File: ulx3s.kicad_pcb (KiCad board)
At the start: 4 copper layers, 94 x 50.8 mm, 119 parts, among them J1 CONN_02X20, J2 CONN_02X20, J3 WIFI_OFF, J4 CONN_02X03, Q1 BC857, Q2 2N7002, U10 S25FL164K0XMFI011, U11 PCA9306DCTR, U2 ESP-32S, U3 AP3429A, U4 AP3429A, U5 AP3429A, U6 FT231XS, U7 PCF8523, U8 MAX11123, U9 MT48LC4M16A2TG, Y1 FNETHE025

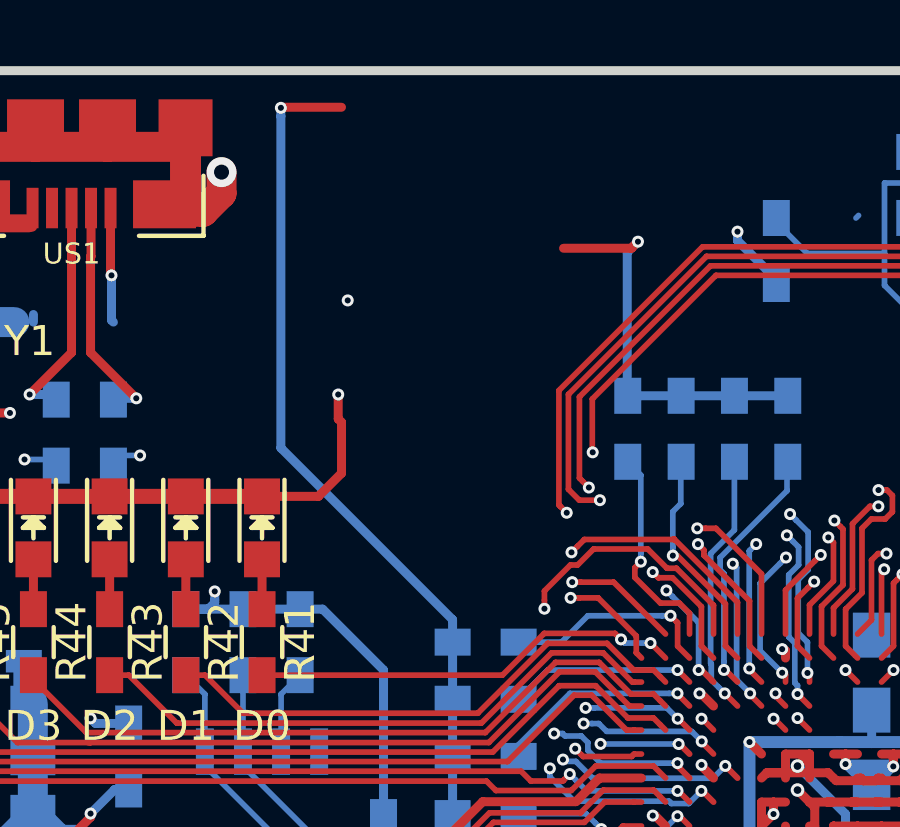
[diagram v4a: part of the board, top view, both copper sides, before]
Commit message: PCB v1.7 fix wrong audio jack connection
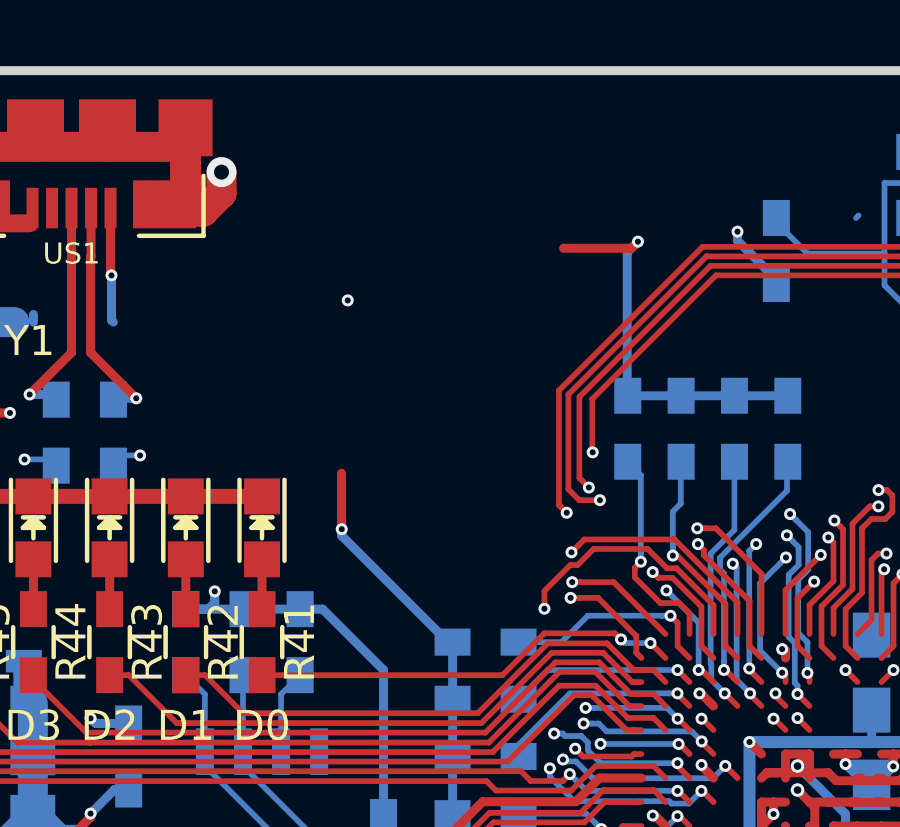
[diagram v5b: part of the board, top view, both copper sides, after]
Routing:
- net /analog/AUDIO_L: track 27.9 -> 13.0 mm
- net GND: track 360.3 -> 354.6 mm, vias 52 -> 51
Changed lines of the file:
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@@
     (links 708)
     (no_connects 0)
-    (area 71.010001 43.48 197.572001 118.732339)
+    (area 93.949999 61.269999 188.230001 112.370001)
     (thickness 1.6)
     (drawings 28)
-    (tracks 4123)
+    (tracks 4115)
     (zones 0)
     (modules 160)
@@
     (fp_line (start -7 -3) (end -5.6 -3) (layer F.SilkS) (width 0.15))
     (pad 1 smd rect (at -6.4 3.7 270) (size 2.2 2.8) (layers F.Cu F.Paste F.Mask)
-      (net 34 /analog/AUDIO_L))
+      (net 1 GND))
     (pad 4 smd rect (at -3.6 3.7 270) (size 2.2 2.8) (layers F.Cu F.Paste F.Mask))
     (pad 2 smd rect (at 5.8 3.7 270) (size 2.8 2.8) (layers F.Cu F.Paste F.Mask)
-      (net 1 GND))
+      (net 34 /analog/AUDIO_L))
     (pad 5 smd rect (at 9.9 -0.75 270) (size 2.8 2.8) (layers F.Cu F.Paste F.Mask))
     (pad 3 smd rect (at -1.7 -3.7 270) (size 2 2.8) (layers F.Cu F.Paste F.Mask)
@@
     (effects (font (size 1.5 1.5) (thickness 0.3)) (justify mirror))
   )
-  (gr_text "ULX3S v1.6" (at 138.55 75.898) (layer F.SilkS)
+  (gr_text "ULX3S v1.7" (at 138.55 75.898) (layer F.SilkS)
     (effects (font (size 1.5 1.5) (thickness 0.3)))
   )
@@
   (segment (start 131.68 89) (end 131.28 89.4) (width 0.3) (layer F.Cu) (net 1))
   (via (at 131.28 89.450837) (size 0.4) (drill 0.2) (layers F.Cu B.Cu) (net 1))
-  (via (at 120.77 72.215) (size 0.4) (drill 0.2) (layers F.Cu B.Cu) (net 1))
-  (segment (start 120.88 74.84) (end 120.88 73.14) (width 0.3) (layer F.Cu) (net 1))
-  (segment (start 120.88 73.14) (end 120.77 73.03) (width 0.3) (layer F.Cu) (net 1))
-  (segment (start 120.77 73.03) (end 120.77 72.215) (width 0.3) (layer F.Cu) (net 1))
   (segment (start 136.126306 93.4) (end 136.095958 93.369652) (width 0.3) (layer B.Cu) (net 1))
   (segment (start 136.095958 93.08681) (end 136.095958 93.369652) (width 0.3) (layer F.Cu) (net 1))
@@
   (segment (start 165.08 82.27) (end 165.08 81.46874) (width 0.3) (layer F.Cu) (net 1))
   (via (at 164.741832 81.130572) (size 0.6) (drill 0.3) (layers F.Cu B.Cu) (net 1))
-  (segment (start 118.23 75.61098) (end 120.10902 75.61098) (width 0.3) (layer F.Cu) (net 1))
-  (segment (start 120.10902 75.61098) (end 120.88 74.84) (width 0.3) (layer F.Cu) (net 1))
   (segment (start 161.08 81.228126) (end 161.067993 81.216119) (width 0.3) (layer F.Cu) (net 1))
   (segment (start 161.08 82.27) (end 161.08 81.228126) (width 0.3) (layer F.Cu) (net 1))
@@
   (segment (start 177.285 77.075) (end 177.285 78.395) (width 0.19) (layer B.Cu) (net 33))
   (segment (start 177.285 78.395) (end 177.115 78.565) (width 0.19) (layer B.Cu) (net 33))
-  (segment (start 124.582 80.47) (end 124.582 79.72) (width 0.3) (layer B.Cu) (net 34))
-  (segment (start 124.582 79.72) (end 118.85869 73.99669) (width 0.3) (layer B.Cu) (net 34))
-  (segment (start 118.85869 62.941812) (end 118.85869 62.65897) (width 0.3) (layer B.Cu) (net 34))
-  (segment (start 118.85869 73.99669) (end 118.85869 62.941812) (width 0.3) (layer B.Cu) (net 34))
-  (segment (start 120.88 62.64) (end 118.87766 62.64) (width 0.3) (layer F.Cu) (net 34))
-  (segment (start 118.87766 62.64) (end 118.85869 62.65897) (width 0.3) (layer F.Cu) (net 34))
-  (via (at 118.85869 62.65897) (size 0.4) (drill 0.2) (layers F.Cu B.Cu) (net 34))
+  (segment (start 120.886867 76.924867) (end 120.886867 76.704249) (width 0.3) (layer B.Cu) (net 34))
+  (segment (start 124.432 80.47) (end 120.886867 76.924867) (width 0.3) (layer B.Cu) (net 34))
+  (segment (start 124.582 80.47) (end 124.432 80.47) (width 0.3) (layer B.Cu) (net 34))
+  (segment (start 120.88 76.697382) (end 120.886867 76.704249) (width 0.3) (layer F.Cu) (net 34))
+  (segment (start 120.88 74.84) (end 120.88 76.697382) (width 0.3) (layer F.Cu) (net 34))
+  (via (at 120.886867 76.704249) (size 0.4) (drill 0.2) (layers F.Cu B.Cu) (net 34))
   (segment (start 124.582 84.279) (end 124.582 86.185) (width 0.3) (layer B.Cu) (net 34))
   (segment (start 124.582 82.375) (end 124.582 84.279) (width 0.3) (layer B.Cu) (net 34))
   (segment (start 124.582 80.47) (end 124.582 82.375) (width 0.3) (layer B.Cu) (net 34))
+  (segment (start 128.28 67.34) (end 130.541611 67.34) (width 0.3) (layer F.Cu) (net 35))
+  (segment (start 130.541611 67.34) (end 130.76199 67.119621) (width 0.3) (layer F.Cu) (net 35))
   (segment (start 132.2 72.258) (end 130.422 72.258) (width 0.3) (layer B.Cu) (net 35))
   (segment (start 133.978 72.258) (end 132.2 72.258) (width 0.3) (layer B.Cu) (net 35))
@@
   (segment (start 130.40294 67.478671) (end 130.76199 67.119621) (width 0.3) (layer B.Cu) (net 35))
   (segment (start 130.40294 72.217) (end 130.40294 67.478671) (width 0.3) (layer B.Cu) (net 35))
-  (segment (start 130.561991 67.31962) (end 130.76199 67.119621) (width 0.3) (layer F.Cu) (net 35))
   (via (at 130.76199 67.119621) (size 0.4) (drill 0.2) (layers F.Cu B.Cu) (net 35))
-  (segment (start 130.541611 67.34) (end 130.561991 67.31962) (width 0.3) (layer F.Cu) (net 35))
-  (segment (start 128.28 67.34) (end 130.541611 67.34) (width 0.3) (layer F.Cu) (net 35))
   (segment (start 148.477832 69.002168) (end 148.167449 68.691785) (width 0.19) (layer B.Cu) (net 36))
   (segment (start 148.167449 68.691785) (end 148.071785 68.691785) (width 0.19) (layer B.Cu) (net 36))

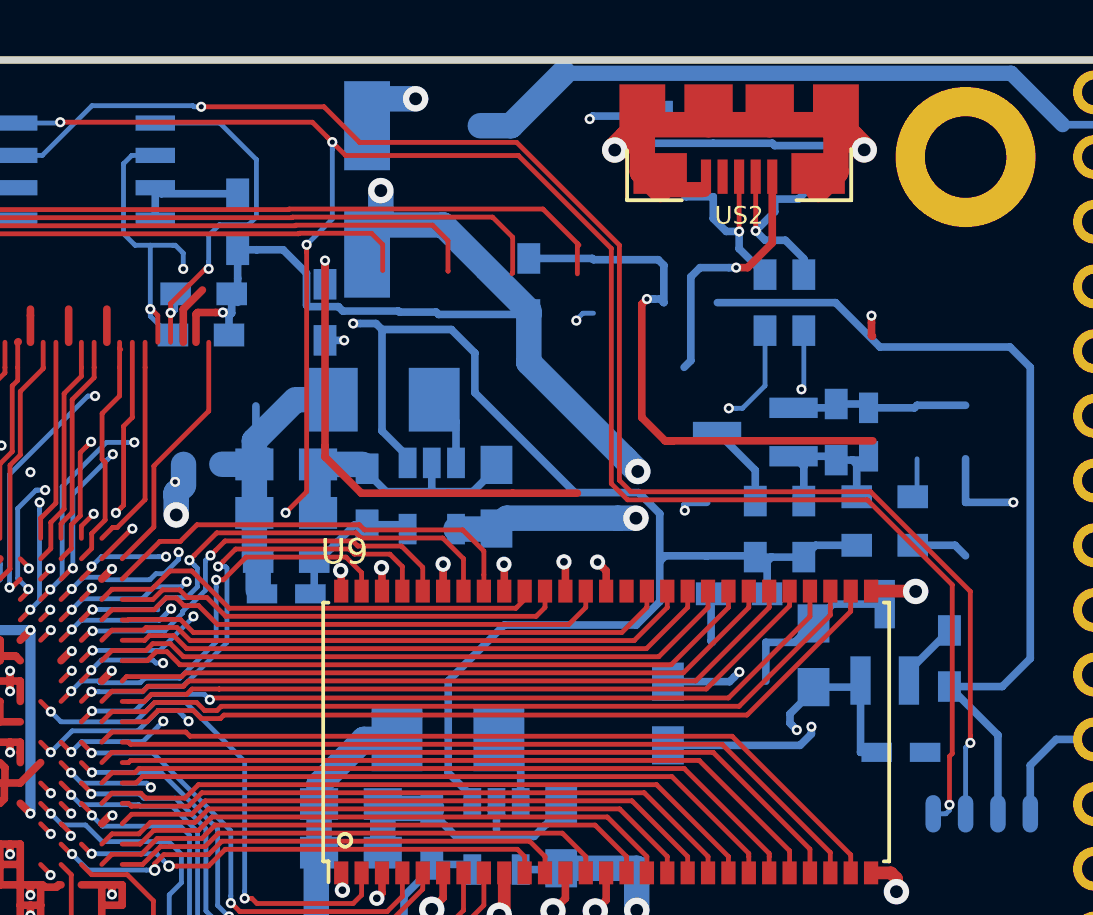
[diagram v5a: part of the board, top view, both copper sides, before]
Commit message: gpdi sheet, i2c voltage shifter, VREF filtering with C18 100nF->470nF
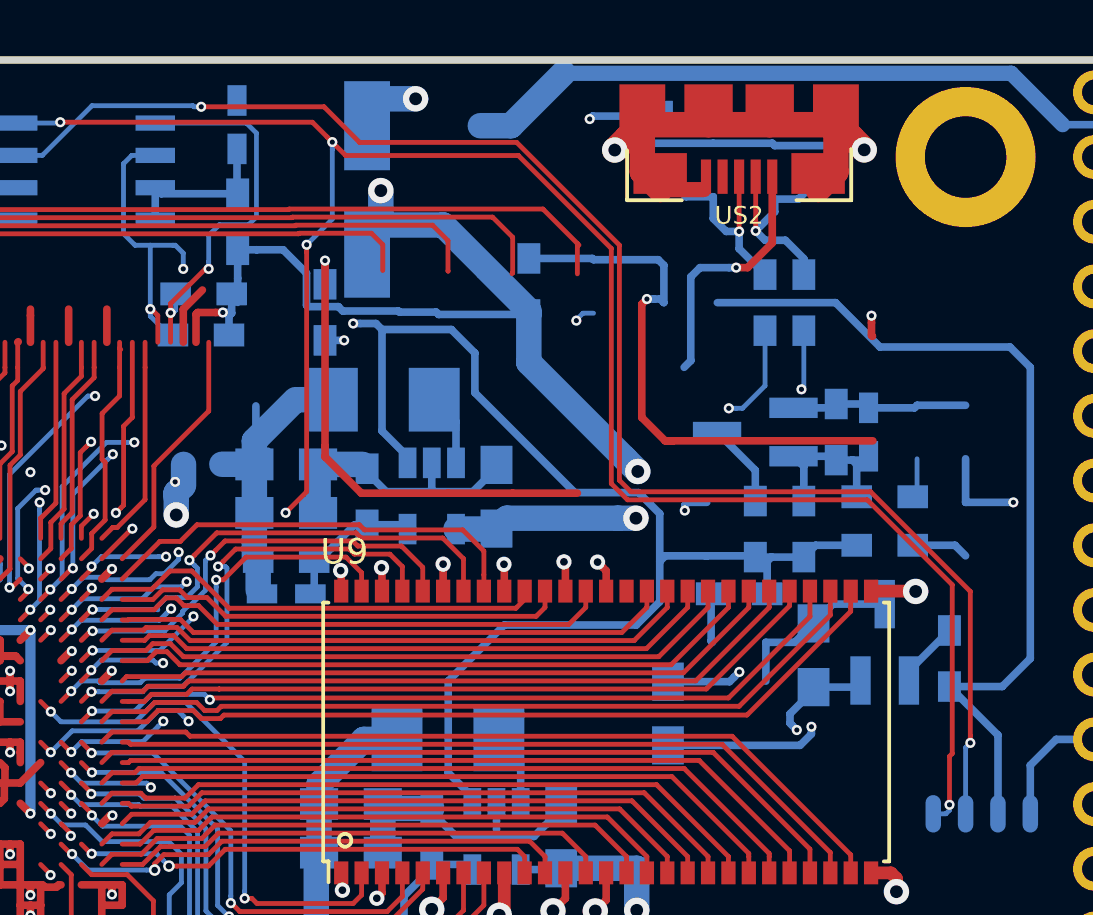
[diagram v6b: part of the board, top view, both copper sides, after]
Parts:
- C18: value 100nF -> 470pF
- moved C18 35.9 mm to (150.6, 64.0), turned to 90 degrees
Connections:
- C18 pad 1: +5V -> /gpdi/VREF2
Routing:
- net +5V: track 207.2 -> 203.8 mm
- net /gpdi/VREF2: track 4.60 -> 6.37 mm
- net GPDI_5V_SDA: track 14.8 -> 15.4 mm
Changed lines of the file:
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@@
   )
   (module Capacitors_SMD:C_0603_HandSoldering (layer B.Cu)
-    (at 176.65 88.598)
+    (at 150.5896 63.96 90)
     (descr "Capacitor SMD 0603, hand soldering")
     (tags "capacitor 0603")
     (attr smd)
-    (fp_text reference C18 (at 3.302 0) (layer B.SilkS)
+    (fp_text reference C18 (at 0 -1.3716 90) (layer B.SilkS)
       (effects (font (size 1 1) (thickness 0.15)) (justify mirror))
     )
-    (fp_text value 100nF (at 4.064 0.508) (layer B.Fab)
+    (fp_text value 470pF (at 4.064 0.508 90) (layer B.Fab)
       (effects (font (size 1 1) (thickness 0.15)) (justify mirror))
     )
@@
     (fp_line (start -0.35 0.6) (end 0.35 0.6) (layer B.SilkS) (width 0.15))
     (fp_line (start 0.35 -0.6) (end -0.35 -0.6) (layer B.SilkS) (width 0.15))
-    (pad 1 smd rect (at -0.95 0) (size 1.2 0.75) (layers B.Cu B.Paste B.Mask)
-      (net 2 +5V))
-    (pad 2 smd rect (at 0.95 0) (size 1.2 0.75) (layers B.Cu B.Paste B.Mask)
+    (pad 1 smd rect (at -0.95 0 90) (size 1.2 0.75) (layers B.Cu B.Paste B.Mask)
+      (net 40 /gpdi/VREF2))
+    (pad 2 smd rect (at 0.95 0 90) (size 1.2 0.75) (layers B.Cu B.Paste B.Mask)
       (net 1 GND))
     (model Capacitors_SMD.3dshapes/C_0603.wrl
@@
     (tags "resistor 0603")
     (attr smd)
-    (fp_text reference R24 (at 3.302 -0.127 90) (layer B.SilkS)
+    (fp_text reference R24 (at 0.508 -1.397 90) (layer B.SilkS)
       (effects (font (size 1 1) (thickness 0.15)) (justify mirror))
     )
@@
   (segment (start 106.546 69.802) (end 106.419 69.929) (width 1) (layer B.Cu) (net 2))
   (segment (start 166.28 94.8) (end 166.28 87.328) (width 1) (layer In1.Cu) (net 2))
-  (segment (start 175.065 88.598) (end 175.065 85.78) (width 0.3) (layer B.Cu) (net 2))
-  (segment (start 175.7 88.598) (end 175.065 88.598) (width 0.3) (layer B.Cu) (net 2))
   (segment (start 106.419 69.929) (end 106.407114 69.940886) (width 1) (layer B.Cu) (net 2))
   (segment (start 106.419 69.675) (end 106.419 69.929) (width 0.3) (layer B.Cu) (net 2))
@@
   (segment (start 147.925 72.215) (end 147.186 71.476) (width 0.19) (layer B.Cu) (net 36))
   (segment (start 148.075 72.215) (end 148.075 71.961) (width 0.19) (layer B.Cu) (net 36))
-  (segment (start 147.38 63.895) (end 149.915 63.895) (width 0.19) (layer B.Cu) (net 37))
-  (segment (start 149.475951 68.307142) (end 149.475951 69.336842) (width 0.19) (layer B.Cu) (net 37))
-  (segment (start 149.915 63.895) (end 151.352044 65.332044) (width 0.19) (layer B.Cu) (net 37))
-  (segment (start 151.352044 65.332044) (end 151.352044 67.579418) (width 0.19) (layer B.Cu) (net 37))
+  (segment (start 147.38 63.895) (end 150.955962 63.895) (width 0.19) (layer B.Cu) (net 37))
+  (segment (start 150.955962 63.895) (end 151.352044 64.291082) (width 0.19) (layer B.Cu) (net 37))
   (segment (start 151.352044 67.579418) (end 151.043301 67.888161) (width 0.19) (layer B.Cu) (net 37))
+  (segment (start 151.352044 64.291082) (end 151.352044 67.579418) (width 0.19) (layer B.Cu) (net 37))
   (segment (start 151.043301 67.888161) (end 149.894932 67.888161) (width 0.19) (layer B.Cu) (net 37))
   (segment (start 149.894932 67.888161) (end 149.475951 68.307142) (width 0.19) (layer B.Cu) (net 37))
+  (segment (start 149.475951 68.307142) (end 149.475951 69.336842) (width 0.19) (layer B.Cu) (net 37))
   (segment (start 149.475951 69.336842) (end 149.475951 69.619684) (width 0.19) (layer B.Cu) (net 37))
   (segment (start 149.475951 69.619684) (end 149.346123 69.619684) (width 0.19) (layer F.Cu) (net 37))
@@
   (via (at 140.035989 81.4) (size 0.4) (drill 0.2) (layers F.Cu B.Cu) (net 39))
   (segment (start 140.035989 81.444011) (end 140.035989 81.4) (width 0.19) (layer F.Cu) (net 39))
+  (segment (start 150.5896 64.91) (end 150.5896 66.6446) (width 0.3) (layer B.Cu) (net 40))
+  (segment (start 150.5896 66.6446) (end 150.615 66.67) (width 0.3) (layer B.Cu) (net 40))
   (segment (start 147.38 67.705) (end 147.38 66.435) (width 0.3) (layer B.Cu) (net 40))
   (segment (start 150.615 66.67) (end 147.615 66.67) (width 0.3) (layer B.Cu) (net 40))

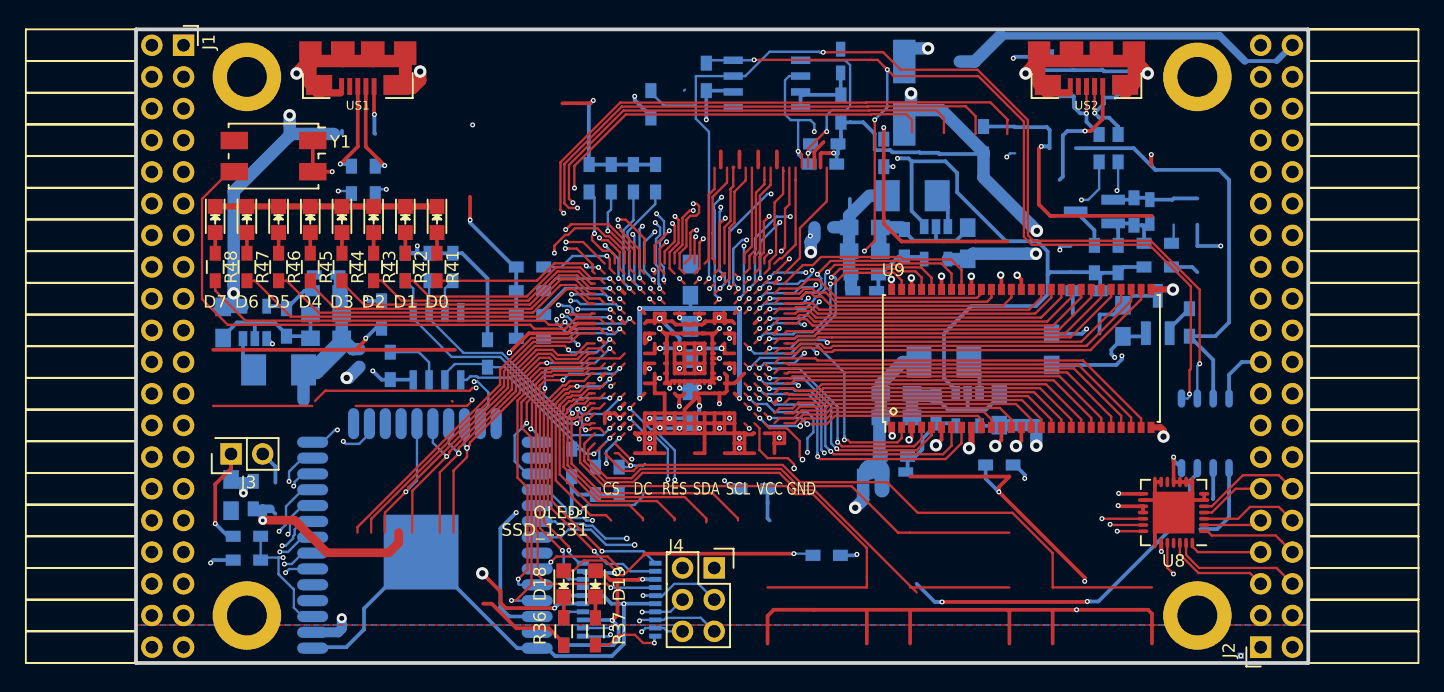
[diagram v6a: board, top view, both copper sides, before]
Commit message: analog: audio ring2 resistor DAC network connected to FPGA copper infill is getting thin, so minimal-thickness traces are used 0.127 mm
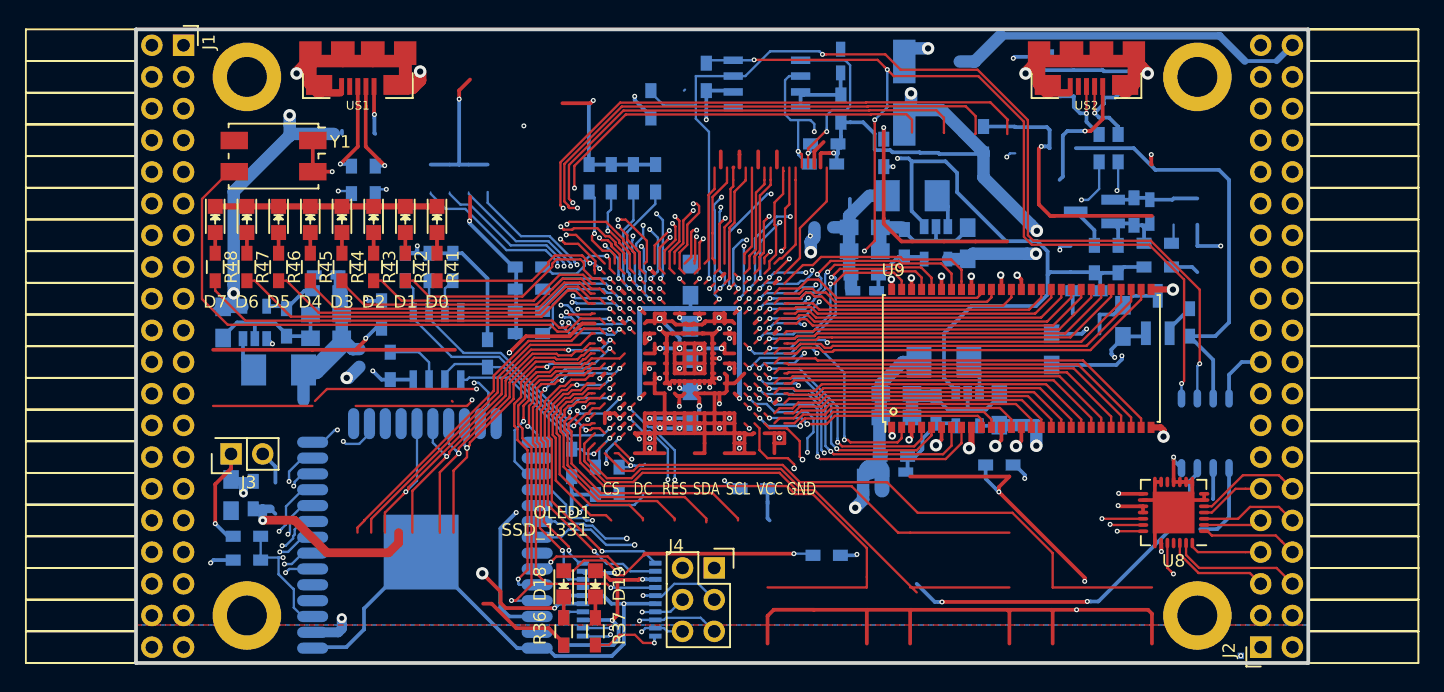
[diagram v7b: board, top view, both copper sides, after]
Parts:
- moved R14 0.39 mm to (125.6, 85.8)
- moved R15 0.27 mm to (125.6, 84.0)
- moved R16 0.15 mm to (125.6, 82.2)
- moved R17 0.09 mm to (125.6, 80.5)
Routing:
- net AUDIO_V3: track 0.00 -> 22.7 mm, vias 0 -> 2
- net AUDIO_V2: track 0.00 -> 19.8 mm, vias 0 -> 2
- net AUDIO_V1: track 0.00 -> 17.7 mm, vias 0 -> 2
- net AUDIO_V0: track 0.00 -> 16.9 mm, vias 0 -> 2
- net /analog/AUDIO_V: track 0.00 -> 11.8 mm, vias 0 -> 1
- net J1_11-: track 52.9 -> 49.3 mm
- net SW2: track 54.8 -> 53.0 mm
- net SW0: track 45.9 -> 47.3 mm, vias 3 -> 2
- net SW1: track 48.9 -> 49.9 mm
- net LED1: track 18.0 -> 19.0 mm
- net /power/PWREN: track 109.5 -> 108.6 mm
- net /flash/FLASH_MOSI: track 15.9 -> 15.0 mm
- net AUDIO_L0: track 7.10 -> 7.86 mm
- net J1_27-: track 45.9 -> 46.7 mm
- net SW3: track 57.5 -> 56.8 mm, vias 2 -> 3
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
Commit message: trac cosmetix
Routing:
- net +3V3: track 306.3 -> 302.6 mm
- net J1_11-: track 49.3 -> 52.5 mm
- net J2_29+: track 51.9 -> 49.1 mm, vias 1 -> 2
- net J2_25+: track 51.5 -> 50.2 mm
- net J2_15-: track 45.3 -> 44.6 mm
